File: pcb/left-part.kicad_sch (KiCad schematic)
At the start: 67 parts, among them J3 MJ-4PP-9, SW1 SW_PUSH, SW10 SW_PUSH, SW11 SW_PUSH, SW12 SW_PUSH, SW13 SW_PUSH, SW14 SW_PUSH, SW15 SW_PUSH, SW16 SW_PUSH, SW17 SW_PUSH, SW18 SW_PUSH, SW19 SW_RESET, SW2 SW_PUSH, SW20 SW_PUSH, SW21 SW_PUSH, SW22 SW_PUSH, SW23 SW_PUSH, SW3 SW_PUSH, SW4 SW_PUSH, SW47 SW_PUSH, SW48 SW_PUSH, SW49 SW_PUSH, SW5 SW_PUSH, SW50 SW_PUSH, SW51 SW_PUSH, SW52 SW_PUSH, SW6 SW_PUSH, SW7 SW_PUSH, SW8 SW_PUSH, SW9 SW_PUSH, U1 Raspberry_Pie_Pico

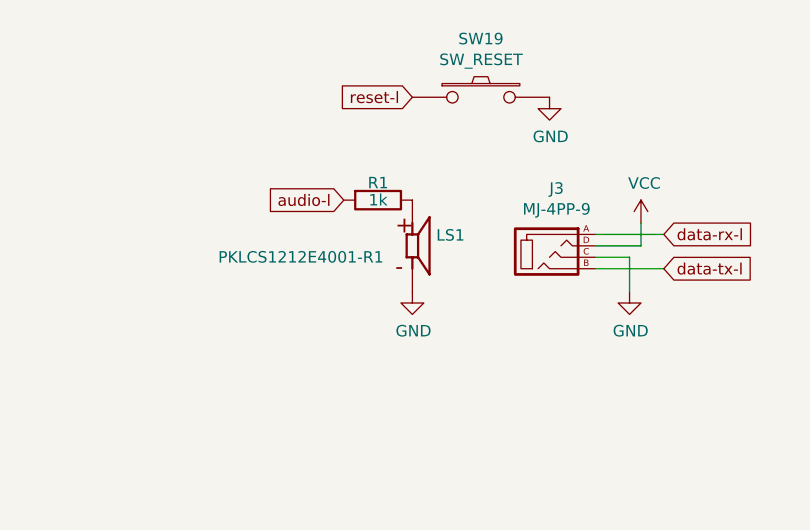
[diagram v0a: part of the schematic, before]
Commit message: fixed schematic ERC errors and warnings refactored some symbols to project-level libraries
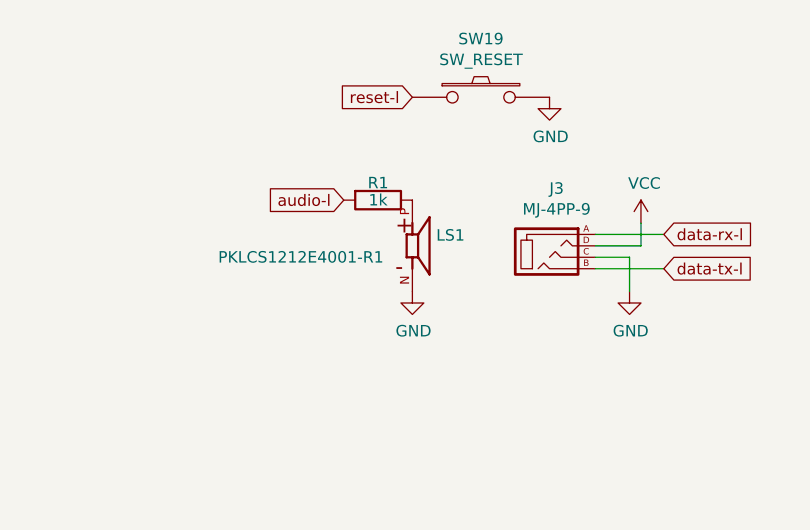
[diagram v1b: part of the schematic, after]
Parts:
- D1, D10, D11, D12, D13, D14, D15, D16, D17, D18, D19, D2, D20, D21, D22, D3, D4, D5, D50, D52, D58, D6, D60, D61, D62, D7, D8, D9: footprint Keebio-Parts:Diode-Hybrid-Back -> _keebio-parts:Diode-Hybrid-Back
- D45, D46, D47, D48, D49, D51: footprint Yoichiro:LED_WS2812B -> _yoichiro:LED_WS2812B
- J3: footprint kbd:MJ-4PP-9_1side -> _kbd:MJ-4PP-9; symbol kbd:MJ-4PP-9 -> _kbd:MJ-4PP-9
- LS1: footprint Yoichiro:SPKR_PKLCS1212E4001-R1 -> _speaker:SPKR_PKLCS1212E4001-R1; symbol PKLCS1212E4001-R1:PKLCS1212E4001-R1 -> _speaker:PKLCS1212E4001-R1; Availability (none) -> In Stock; Check_prices (none) -> https://www.snapeda.com/parts/PKLCS1212E4001-R1/Murata/view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; Description_1 (none) -> Buzzers Transducer, Externally Driven Piezo 1.5 V - 4kHz 84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; MANUFACTURER (none) -> Murata Electronics; MAXIMUM_PACKAGE_HEIGHT (none) -> 3.0 mm; MF (none) -> Murata; MP (none) -> PKLCS1212E4001-R1; PARTREV (none) -> January 22, 2018; Package (none) -> SMD-2 Murata; Price (none) -> None; Purchase-URL (none) -> https://www.snapeda.com/api/url_track_click_mouser/?unipart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; STANDARD (none) -> Manufacturer Recommendations; SnapEDA_Link (none) -> https://www.snapeda.com/parts/PKLCS1212E4001-R1/Murata/view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
- R1: footprint Keebio-Parts:Resistor-Hybrid-Back -> _keebio-parts:Resistor-Hybrid-Back
- SW1, SW10, SW11, SW12, SW13, SW14, SW15, SW16, SW17, SW18, SW2, SW20, SW21, SW22, SW23, SW3, SW4, SW47, SW48, SW49, SW5, SW50, SW51, SW52, SW6, SW7, SW8, SW9: footprint Yoichiro:CherryMX_Choco_Hotswap -> _yoichiro:CherryMX_Choco_Hotswap; symbol kbd:SW_PUSH -> _kbd:SW_PUSH
- SW19: footprint kbd:ResetSW_1side -> _kbd:ResetSW; symbol kbd:SW_PUSH -> _kbd:SW_PUSH
- U1: footprint Yoichiro:Raspberry_Pi_Pico -> _yoichiro:Raspberry_Pi_Pico; symbol yoichiro:Raspberry_Pie_Pico -> _yoichiro:Raspberry_Pi_Pico
